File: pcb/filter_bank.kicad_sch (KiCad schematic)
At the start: 56 parts, among them K1 G6K-2F-Y-DC5, K2 G6K-2F-Y-DC5, K3 G6K-2F-Y-DC5, K4 G6K-2F-Y-DC5, K5 G6K-2F-Y-DC5, K6 G6K-2F-Y-DC5, Q6 AO3400A, Q7 AO3400A

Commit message: BOM: fill MPN/Manufacturer/LCSC for 47 Rev B parts (Basic preferred; C3 10u/25V, C7 1u/50V, C11 100n/50V). Hand-solder parts J11, Q3, Q8, DS1, L2 marked Assembly=hand solder and excluded from pos files. Nets unchanged, ERC 0 errors
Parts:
- C407: LCSC (none) -> C519097; MPN (none) -> CC0603BRNPO9BN1R1; Manufacturer (none) -> YAGEO
- L201, L202: LCSC (none) -> C6645233; MPN 1008CS-152XJLC -> 1008CS-152XGRC
- L203: LCSC (none) -> C40228699; MPN 1008CS-182XJLC -> 1008CS-182XGLC
- L402: LCSC (none) -> C5471933; MPN 1008CS-561XJLC -> 1008CS-561XJRC
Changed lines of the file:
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@@
 			)
 		)
-		(property "MPN" "1008CS-152XJLC"
+		(property "MPN" "1008CS-152XGRC"
 			(at 44.45 38.1 0)
 			(effects
@@
 			)
 		)
+		(property "LCSC" "C6645233"
+			(at 44.45 34.8 90)
+			(effects
+				(font
+					(size 1.27 1.27)
+				)
+				(hide yes)
+			)
+		)
 		(pin "1"
 		)
@@
 			)
 		)
-		(property "MPN" "1008CS-152XJLC"
+		(property "MPN" "1008CS-152XGRC"
 			(at 67.31 38.1 0)
 			(effects
@@
 			)
 		)
+		(property "LCSC" "C6645233"
+			(at 67.31 34.8 90)
+			(effects
+				(font
+					(size 1.27 1.27)
+				)
+				(hide yes)
+			)
+		)
 		(pin "1"
 		)
@@
 			)
 		)
-		(property "MPN" "1008CS-182XJLC"
+		(property "MPN" "1008CS-182XGLC"
 			(at 90.17 38.1 0)
 			(effects
@@
 		(property "Manufacturer" "Coilcraft"
 			(at 90.17 38.1 0)
+			(effects
+				(font
+					(size 1.27 1.27)
+				)
+				(hide yes)
+			)
+		)
+		(property "LCSC" "C40228699"
+			(at 90.17 34.8 90)
 			(effects
 				(font
@@
 			)
 		)
+		(property "MPN" "CC0603BRNPO9BN1R1"
+			(at 103.505 100.33 0)
+			(effects
+				(font
+					(size 1.27 1.27)
+				)
+				(hide yes)
+			)
+		)
+		(property "Manufacturer" "YAGEO"
+			(at 103.505 100.33 0)
+			(effects
+				(font
+					(size 1.27 1.27)
+				)
+				(hide yes)
+			)
+		)
+		(property "LCSC" "C519097"
+			(at 103.505 100.33 0)
+			(effects
+				(font
+					(size 1.27 1.27)
+				)
+				(hide yes)
+			)
+		)
 		(pin "1"
 		)
@@
 			)
 		)
-		(property "MPN" "1008CS-561XJLC"
+		(property "MPN" "1008CS-561XJRC"
 			(at 67.31 99.06 0)
 			(effects
@@
 			(effects
 				(font
+					(size 1.27 1.27)
+				)
+				(hide yes)
+			)
+		)
+		(property "LCSC" "C5471933"
+			(at 67.31 95.76 90)
+			(effects
+				(font

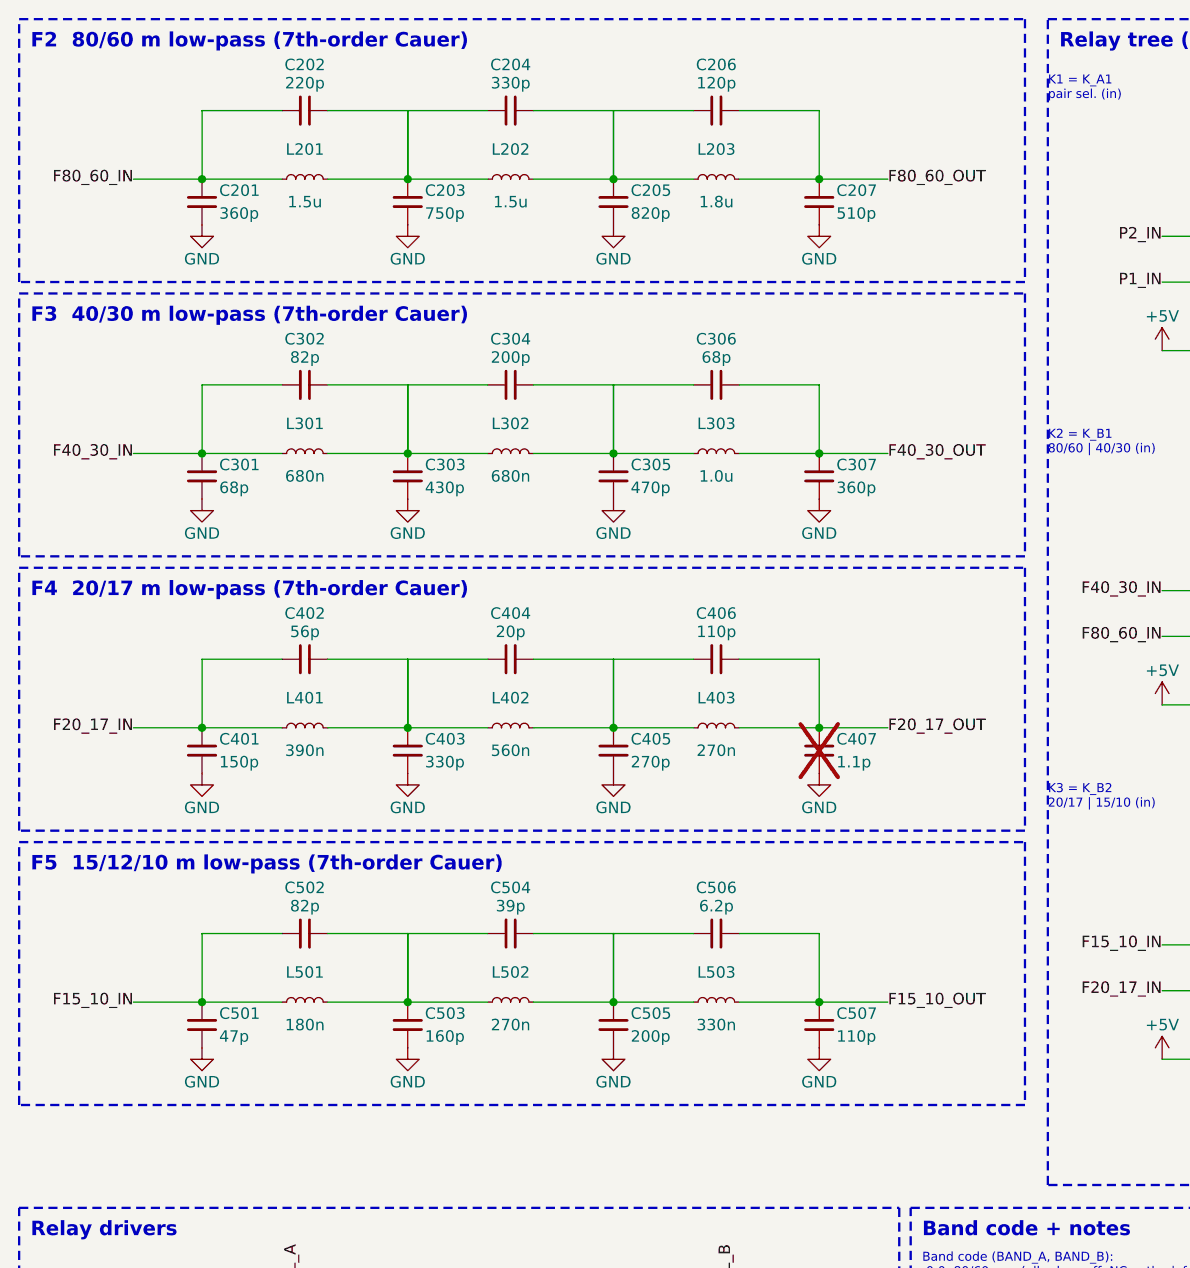
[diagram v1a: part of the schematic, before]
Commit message: LPF F2-F5: hand-wound T30 toroid design (1 W max); L1/C3 part swaps
- Move F2-F5 to new nested A4 sheet "LPF Filters" (lpf_filters.kicad_sch),
  instantiated from Filter Bank; same F*_IN/F*_OUT nets to the relay tree.
- 12 inductors -> hand-wound Micrometals T30-2 (F2/F3) / T30-6 (F4/F5),
  values/turns/wire per ob2_filters/t30 design. Fields: Core, Turns, Wire,
  MPN=T30-x, Supplier=Kits and Parts. DNP, excluded from pos files, no LCSC.
  Footprint Inductor_THT:L_Toroid_Vertical_L10.0mm_W5.0mm_P5.08mm.
- All filter caps 0603 C0G/NP0 50 V JLC Basic/preferred, parallel combos
  as designed (C208+ etc.). C406/C407/C507 kept (still used; C407 now fitted).
- Winding table + notes on the LPF sheet.
- L1 -> Sunlord MWSA0402S-100MT (C408339), existing Murata100M pads fit.
- C3 -> Samsung CL31A106KBHNNNE (C13585), 1206 footprint.
- ERC 0 errors; netlist matches simulated topology node for node.
- Regenerate docs/OpenBeacon2_schematic.pdf.
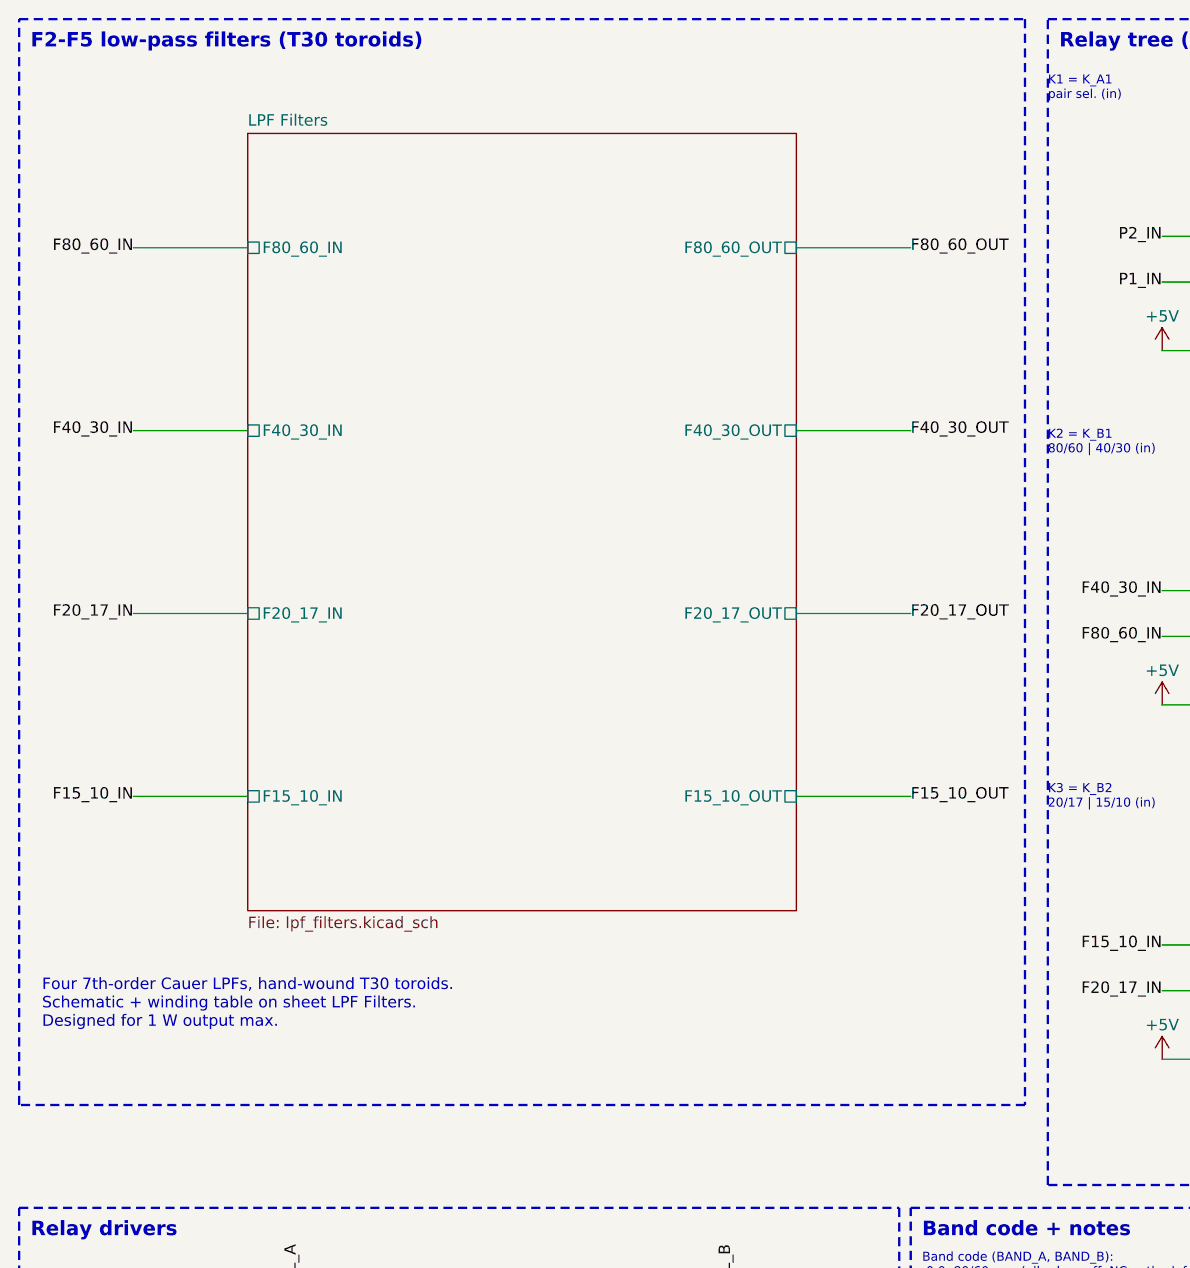
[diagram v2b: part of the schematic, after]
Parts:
- removed C201, C307: 360p, Capacitor_SMD:C_0603_1608Metric, symbol Device:C_Small
- removed C202: 220p, Capacitor_SMD:C_0603_1608Metric, symbol Device:C_Small
- removed C203: 750p, Capacitor_SMD:C_0603_1608Metric, symbol Device:C_Small
- removed C204, C403: 330p, Capacitor_SMD:C_0603_1608Metric, symbol Device:C_Small
- removed C205: 820p, Capacitor_SMD:C_0603_1608Metric, symbol Device:C_Small
- removed C206: 120p, Capacitor_SMD:C_0603_1608Metric, symbol Device:C_Small
- removed C207: 510p, Capacitor_SMD:C_0603_1608Metric, symbol Device:C_Small
- removed C301, C306: 68p, Capacitor_SMD:C_0603_1608Metric, symbol Device:C_Small
- removed C302, C502: 82p, Capacitor_SMD:C_0603_1608Metric, symbol Device:C_Small
- removed C303: 430p, Capacitor_SMD:C_0603_1608Metric, symbol Device:C_Small
- removed C304, C505: 200p, Capacitor_SMD:C_0603_1608Metric, symbol Device:C_Small
- removed C305: 470p, Capacitor_SMD:C_0603_1608Metric, symbol Device:C_Small
- removed C401: 150p, Capacitor_SMD:C_0603_1608Metric, symbol Device:C_Small
- removed C402: 56p, Capacitor_SMD:C_0603_1608Metric, symbol Device:C_Small
- removed C404: 20p, Capacitor_SMD:C_0603_1608Metric, symbol Device:C_Small
- removed C405: 270p, Capacitor_SMD:C_0603_1608Metric, symbol Device:C_Small
- removed C406, C507: 110p, Capacitor_SMD:C_0603_1608Metric, symbol Device:C_Small
- removed C407: 1.1p, Capacitor_SMD:C_0603_1608Metric, symbol Device:C_Small
- removed C501: 47p, Capacitor_SMD:C_0603_1608Metric, symbol Device:C_Small
- removed C503: 160p, Capacitor_SMD:C_0603_1608Metric, symbol Device:C_Small
- removed C504: 39p, Capacitor_SMD:C_0603_1608Metric, symbol Device:C_Small
- removed C506: 6.2p, Capacitor_SMD:C_0603_1608Metric, symbol Device:C_Small
- removed L201, L202: 1.5u, Inductor_SMD:L_1008_2520Metric, symbol Device:L_Small
- removed L203: 1.8u, Inductor_SMD:L_1008_2520Metric, symbol Device:L_Small
- removed L301, L302: 680n, Inductor_SMD:L_1008_2520Metric, symbol Device:L_Small
- removed L303: 1.0u, Inductor_SMD:L_1008_2520Metric, symbol Device:L_Small
- removed L401: 390n, Inductor_SMD:L_1008_2520Metric, symbol Device:L_Small
- removed L402: 560n, Inductor_SMD:L_1008_2520Metric, symbol Device:L_Small
- removed L403, L502: 270n, Inductor_SMD:L_1008_2520Metric, symbol Device:L_Small
- removed L501: 180n, Inductor_SMD:L_1008_2520Metric, symbol Device:L_Small
- removed L503: 330n, Inductor_SMD:L_1008_2520Metric, symbol Device:L_Small
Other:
- added sheet LPF Filters (lpf_filters.kicad_sch)
- note added: "F2-F5 low-pass filters (T30 toroids)"
- note added: "Four 7th-order Cauer LPFs, hand-wound T30 toroids. Schematic + winding table on sheet LPF Filters. Designed for 1 W output max."
- note removed: "F2 80/60 m low-pass (7th-order Cauer)"
- note removed: "F3 40/30 m low-pass (7th-order Cauer)"
- note removed: "F4 20/17 m low-pass (7th-order Cauer)"
- note removed: "F5 15/12/10 m low-pass (7th-order Cauer)"

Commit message: Rev C layout: board grown to 130x110 mm, headers J4/J5/J8/J10/J14 removed, power rework layout
- Outline grown 10 mm on top and left edges (130x110 mm); locked edge parts moved with outline
- Removed J4, J5, J8, J10, J14 and support parts (D13-D15, D17, D19, D20, R64-R67, R69-R71, R75-R79); UPDI J13 kept
- Power rework placed and routed (TPS61085 boost, INA193 U14, Q10 soft-start)
- Y1 placed at U9, stray passives moved, silkscreen labels cleaned up
- Routed: DRC 0 errors / 0 unconnected, schematic parity 0, ERC 0; layout gate 11/11
- DRU: ESC_* fine-pitch escape 0.20 mm rule areas, U1 pad-to-pad 0.14 mm
- In2 keep-away waivers (GND-plane shielded): Q2 drain, MCU_TX, MCU_RX near R6, 22.6 mm MCU_RX run near U9
- Libs: 6x6 H13 switch, OLED pin-header module footprint, updated symbols
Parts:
- added Q9: AO3400A, Package_TO_SOT_SMD:SOT-23, symbol Transistor_FET:2N7002
- added R91: 22k, Resistor_SMD:R_0603_1608Metric, symbol Device:R_Small_US
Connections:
- net COIL_B: no longer D3.2 (A), D6.2 (A), K3.8, K6.8
- net GND: now also Q9.2 (S), R91.2
- new net BAND_C: Q9.1 (G), R91.1
- new net COIL_C: D3.2 (A), D6.2 (A), K3.8, K6.8, Q9.3 (D)
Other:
- note added: "BAND_A -> K1/K4, BAND_B -> K2/K5, BAND_C -> K3/K6. Q6 (BAND_A): 2 coils, 42 mA nom (5 V / 237 R), <= 49 mA at 5.25 V, -10 % coil R. Q7 (BAND_B), Q9 (BAND_C): 2 coils each, 42 mA nom, <= 49 mA. AO3400A: 5.7 A cont., 48 mR @ Vgs 2.5 V -> <5 mV drop. One 1N4148W flyback per coil, at each relay."
- note added: "Band code (BAND_A, BAND_B, BAND_C): 0 0 0 80/60 m (all relays off, NC path, default) 0 1 0 40/30 m (K2, K5 on) 1 0 0 20/17 m (K1, K4 on) 1 0 1 15/12/10 m (K1, K4, K3, K6 on) Other codes unused; never more than 4 coils on. Unselected filters float (open at both ends). +5V relay load: 0 / 42 / 42 / 84 mA nominal (<=98 mA worst). Relay pins: COM right, NC lower left, NO upper left; pole 2 unused. In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"
- note removed: "BAND_A -> K1/K4, BAND_B -> K2/K3/K5/K6. Q6 (BAND_A): 2 coils, 42 mA nom (5 V / 237 R), <= 49 mA at 5.25 V, -10 % coil R. Q7 (BAND_B): 4 coils, 84 mA nom, <= 98 mA. AO3400A: 5.7 A cont., 48 mR @ Vgs 2.5 V -> <5 mV drop. One 1N4148W flyback per coil, at each relay."
- note removed: "Band code (BAND_A, BAND_B): 0 0 80/60 m (all relays off, NC path, default) 0 1 40/30 m (K2, K3, K5, K6 on) 1 0 20/17 m (K1, K4 on) 1 1 15/12/10 m (all six on) Unselected filters float (open at both ends). +5V relay load: 0 / 84 / 42 / 127 mA nominal (<=147 mA). Relay pins: COM right, NC lower left, NO upper left; pole 2 unused. Input and output paths never share a relay body. Layout: keep K1-K2-K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"
